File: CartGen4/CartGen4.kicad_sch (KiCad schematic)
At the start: 0 parts

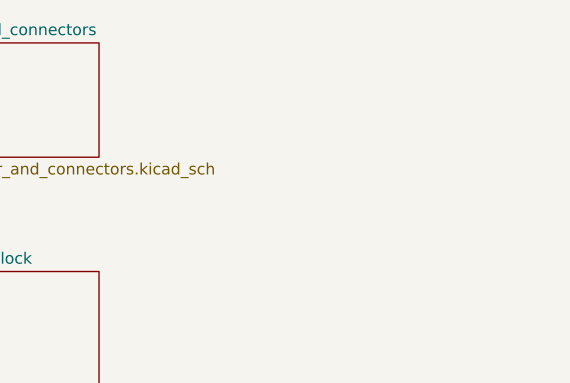
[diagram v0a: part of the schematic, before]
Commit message: Added GB_AUDIO to expansion port
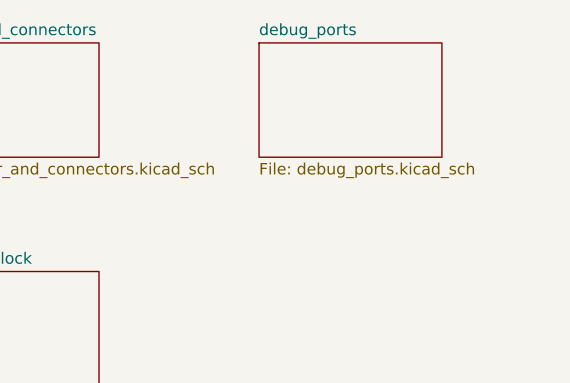
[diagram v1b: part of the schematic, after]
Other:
- added sheet debug_ports (debug_ports.kicad_sch)
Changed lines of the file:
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@@
     (company "© Elijah Almeida Coimbra")
+  )
+  (sheet (at 63.5 38.1) (size 20.32 12.7) (fields_autoplaced)
+    (stroke (width 0.1524) (type solid) (color 0 0 0 0))
+    (fill (color 0 0 0 0.0000))
+    (property "Sheet name" "debug_ports" (id 0) (at 63.5 37.3884 0)
+      (effects (font (size 1.27 1.27)) (justify left bottom))
+    )
+    (property "Sheet file" "debug_ports.kicad_sch" (id 1) (at 63.5 51.3846 0)
+      (effects (font (size 1.27 1.27)) (justify left top))
+    )
   )
   (sheet (at 25.4 38.1) (size 20.32 12.7) (fields_autoplaced)
@@
     (path "/a842574a-62bd-4545-b3b1-b3137c6c2721" (page "7"))
     (path "/c0de9d84-51e9-4175-bb13-3213096ac344" (page "8"))
+    (path "/36ce4ffd-44e6-403f-b850-25c002dce5eb" (page "9"))
   )
   (symbol_instances
@@
       (reference "#PWR015") (unit 1) (value "GND") (footprint "")
     )
-    (path "/4ef07d45-f940-4cb6-bb96-2ddec13fd099/29405421-cb76-4eb6-9e9f-fff247a228fb"
+    (path "/4ef07d45-f940-4cb6-bb96-2ddec13fd099/4f06e38f-fb7c-4d1b-860e-fcc3c051f845"
       (reference "#PWR016") (unit 1) (value "GND") (footprint "")
     )
@@
       (reference "#PWR064") (unit 1) (value "GND") (footprint "")
     )
+    (path "/36ce4ffd-44e6-403f-b850-25c002dce5eb/93aa40b6-bef5-42fa-8e30-902e4ca42004"
+      (reference "#PWR065") (unit 1) (value "GND") (footprint "")
+    )
     (path "/89c162de-8374-4cb6-9c74-abac2a052a8d/6c3a4a37-01ca-4bdc-8d1b-7ba403960e15"
       (reference "#PWR066") (unit 1) (value "+1V8") (footprint "")
@@
       (reference "#PWR067") (unit 1) (value "GND") (footprint "")
     )
+    (path "/36ce4ffd-44e6-403f-b850-25c002dce5eb/29405421-cb76-4eb6-9e9f-fff247a228fb"
+      (reference "#PWR068") (unit 1) (value "GND") (footprint "")
+    )
+    (path "/36ce4ffd-44e6-403f-b850-25c002dce5eb/ef58feb6-b488-41d3-99c3-65a2164e4cd6"
+      (reference "#PWR069") (unit 1) (value "+3.3V") (footprint "")
+    )
     (path "/89c162de-8374-4cb6-9c74-abac2a052a8d/1e8f1802-5e65-4a38-a899-cb4ea4774e61"
       (reference "#PWR070") (unit 1) (value "+3V3") (footprint "")
@@
       (reference "#PWR096") (unit 1) (value "GND") (footprint "")
     )
-    (path "/4ef07d45-f940-4cb6-bb96-2ddec13fd099/93aa40b6-bef5-42fa-8e30-902e4ca42004"
-      (reference "#PWR098") (unit 1) (value "GND") (footprint "")
-    )
     (path "/a842574a-62bd-4545-b3b1-b3137c6c2721/b6280de6-3c34-4640-868d-ea1ae178502d"
       (reference "#PWR0101") (unit 1) (value "GND") (footprint "")
@@
       (reference "#PWR0111") (unit 1) (value "+1V8") (footprint "")
     )
-    (path "/4ef07d45-f940-4cb6-bb96-2ddec13fd099/ef58feb6-b488-41d3-99c3-65a2164e4cd6"
-      (reference "#PWR0112") (unit 1) (value "+3.3V") (footprint "")
-    )
     (path "/4ef07d45-f940-4cb6-bb96-2ddec13fd099/1b8d5810-67b5-41f5-a4e9-e6c2cc9fec50"
       (reference "A1") (unit 1) (value "GBC_Cart") (footprint "Boards:GBC_Cart")
@@
       (reference "C39") (unit 1) (value "100n") (footprint "Capacitor_SMD:C_0402_1005Metric_Pad0.74x0.62mm_HandSolder")
     )
+    (path "/4ef07d45-f940-4cb6-bb96-2ddec13fd099/8d993b11-e0c7-4377-9064-b6937c1178b0"
+      (reference "C40") (unit 1) (value "100n") (footprint "Capacitor_SMD:C_0603_1608Metric_Pad1.08x0.95mm_HandSolder")
+    )
     (path "/76bc839d-93e8-4c60-b95d-ac552335ae99/18009ba6-fe8f-48ae-b5c0-f735d659a1e6"
       (reference "D1") (unit 1) (value "PESD3V3Y1BSFYL") (footprint "SamacSys_Parts:PESD3V3Y1BSFYL")
@@
       (reference "J1") (unit 1) (value "MEM2080-00-128-00-A") (footprint "SamacSys_Parts:MEM2080-00-128-00-A")
     )
-    (path "/4ef07d45-f940-4cb6-bb96-2ddec13fd099/d341df74-d404-4c0e-bfeb-d0bcd9f4785d"
+    (path "/36ce4ffd-44e6-403f-b850-25c002dce5eb/d341df74-d404-4c0e-bfeb-d0bcd9f4785d"
       (reference "J2") (unit 1) (value "Conn_01x05_Male") (footprint "Connector_PinHeader_1.00mm:PinHeader_1x05_P1.00mm_Vertical")
     )
-    (path "/4ef07d45-f940-4cb6-bb96-2ddec13fd099/f15d430b-6a9c-44ac-884d-e5b89d2c844b"
+    (path "/36ce4ffd-44e6-403f-b850-25c002dce5eb/f15d430b-6a9c-44ac-884d-e5b89d2c844b"
       (reference "J3") (unit 1) (value "Conn_02x09_Odd_Even") (footprint "Connector_PinHeader_1.00mm:PinHeader_2x09_P1.00mm_Vertical")
     )
@@
       (reference "R18") (unit 1) (value "15K") (footprint "Resistor_SMD:R_0402_1005Metric_Pad0.72x0.64mm_HandSolder")
     )
+    (path "/4ef07d45-f940-4cb6-bb96-2ddec13fd099/08688eb2-6662-41ab-80a7-03c187b5b46a"
+      (reference "R19") (unit 1) (value "220K") (footprint "Resistor_SMD:R_0402_1005Metric_Pad0.72x0.64mm_HandSolder")
+    )
     (path "/76bc839d-93e8-4c60-b95d-ac552335ae99/de85eafd-55d7-4f64-93d1-ad7e53577dee"
